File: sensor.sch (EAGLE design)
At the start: 16 parts

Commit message: sensor: pcb route completed
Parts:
- removed D1: (no value), SparkFun-DiscreteSemi:DIODESMA
- added SCHOTTKEY: 0, SparkFun-Resistors:10KOHM1/10W1%(0603)0603
- APDS1: device mylib:APDS-9008 -> librae:APDS-9008
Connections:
- net VCC: now also SCHOTTKEY.2; no longer D1.A
- net VDD: now also SCHOTTKEY.1; no longer D1.C
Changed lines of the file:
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@@
 </classes>
 <parts>
-<part name="APDS1" library="mylib" deviceset="APDS-9008" device=""/>
 <part name="MCP6001" library="SparkFun-AnalogIC" deviceset="OPA344" device=""/>
 <part name="C1" library="SparkFun-Capacitors" deviceset="1.0UF-16V-10%(0603)" device="" value="4.7uF"/>
@@
 <part name="R4" library="SparkFun-Resistors" deviceset="10KOHM1/10W1%(0603)" device="0603" value="100K"/>
 <part name="R5" library="SparkFun-Resistors" deviceset="10KOHM1/10W1%(0603)" device="0603" value="10K"/>
-<part name="D1" library="SparkFun-DiscreteSemi" deviceset="DIODE" device="SMA"/>
 <part name="R6" library="SparkFun-Resistors" deviceset="10KOHM1/10W1%(0603)" device="0603" value="3.3M">
 <attribute name="PROD_ID" value="RES-00824"/>
@@
 <part name="GND1" library="SparkFun-Aesthetics" deviceset="GND" device=""/>
 <part name="SUPPLY1" library="SparkFun-Aesthetics" deviceset="VCC" device=""/>
+<part name="SCHOTTKEY" library="SparkFun-Resistors" deviceset="10KOHM1/10W1%(0603)" device="0603" value="0">
+<attribute name="PROD_ID" value="RES-00824"/>
+<attribute name="VALUE" value="10K"/>
+</part>
+<part name="APDS1" library="librae" deviceset="APDS-9008" device=""/>
 </parts>
 <sheets>
@@
 </plain>
 <instances>
-<instance part="APDS1" gate="G$1" x="-38.1" y="17.78" rot="R90"/>
 <instance part="MCP6001" gate="G$1" x="45.72" y="10.16"/>
 <instance part="C1" gate="G$1" x="-7.62" y="-7.62"/>
@@
 <instance part="R4" gate="G$1" x="27.94" y="27.94" rot="R90"/>
 <instance part="R5" gate="G$1" x="10.16" y="27.94" rot="R270"/>
-<instance part="D1" gate="G$1" x="48.26" y="45.72" rot="R180"/>
 <instance part="R6" gate="G$1" x="43.18" y="38.1"/>
 <instance part="JP1" gate="G$1" x="81.28" y="48.26" rot="R180"/>
@@
 <instance part="GND1" gate="1" x="-7.62" y="-22.86"/>
 <instance part="SUPPLY1" gate="1" x="53.34" y="55.88"/>
+<instance part="SCHOTTKEY" gate="G$1" x="48.26" y="45.72"/>
+<instance part="APDS1" gate="G$1" x="-38.1" y="17.78" rot="R90"/>
 </instances>
 <busses>
@@
 <wire x1="-60.96" y1="50.8" x2="-78.74" y2="50.8" width="0.1524" layer="91"/>
 <wire x1="-78.74" y1="50.8" x2="-78.74" y2="20.32" width="0.1524" layer="91"/>
-<pinref part="D1" gate="G$1" pin="A"/>
 <wire x1="50.8" y1="45.72" x2="53.34" y2="45.72" width="0.1524" layer="91"/>
 <wire x1="53.34" y1="45.72" x2="53.34" y2="50.8" width="0.1524" layer="91"/>
@@
 <pinref part="SUPPLY1" gate="1" pin="VCC"/>
 <wire x1="53.34" y1="50.8" x2="53.34" y2="55.88" width="0.1524" layer="91"/>
+<pinref part="SCHOTTKEY" gate="G$1" pin="2"/>
 </segment>
 </net>
 <net name="VDD" class="0">
 <segment>
-<pinref part="APDS1" gate="G$1" pin="1"/>
 <wire x1="-43.18" y1="12.7" x2="-45.72" y2="12.7" width="0.1524" layer="91"/>
 <wire x1="-45.72" y1="12.7" x2="-45.72" y2="20.32" width="0.1524" layer="91"/>
-<pinref part="D1" gate="G$1" pin="C"/>
 <wire x1="-45.72" y1="20.32" x2="-45.72" y2="45.72" width="0.1524" layer="91"/>
-<wire x1="-45.72" y1="45.72" x2="45.72" y2="45.72" width="0.1524" layer="91"/>
+<wire x1="-45.72" y1="45.72" x2="43.18" y2="45.72" width="0.1524" layer="91"/>
 <pinref part="MCP6001" gate="G$1" pin="V+"/>
 <wire x1="45.72" y1="17.78" x2="45.72" y2="20.32" width="0.1524" layer="91"/>
 <wire x1="45.72" y1="20.32" x2="-45.72" y2="20.32" width="0.1524" layer="91"/>
 <junction x="-45.72" y="20.32"/>
+<pinref part="SCHOTTKEY" gate="G$1" pin="1"/>
+<pinref part="APDS1" gate="G$1" pin="1"/>
 </segment>
 </net>
@@
 <net name="N$7" class="0">
 <segment>
-<pinref part="APDS1" gate="G$1" pin="4"/>
 <wire x1="-30.48" y1="7.62" x2="-25.4" y2="7.62" width="0.1524" layer="91"/>
 <pinref part="C2" gate="G$1" pin="2"/>
@@
 <pinref part="R2" gate="G$1" pin="2"/>
 <wire x1="-25.4" y1="-2.54" x2="-25.4" y2="7.62" width="0.1524" layer="91"/>
+<pinref part="APDS1" gate="G$1" pin="4"/>
 </segment>
 </net>
@@
 <junction x="-45.72" y="-17.78"/>
 <wire x1="-45.72" y1="7.62" x2="-45.72" y2="-17.78" width="0.1524" layer="91"/>
-<pinref part="APDS1" gate="G$1" pin="3"/>
 <wire x1="-43.18" y1="7.62" x2="-45.72" y2="7.62" width="0.1524" layer="91"/>
 <wire x1="-25.4" y1="-17.78" x2="-7.62" y2="-17.78" width="0.1524" layer="91"/>
@@
 <junction x="-7.62" y="-17.78"/>
 <junction x="-25.4" y="-17.78"/>
-</segment>
-</net>
+<pinref part="APDS1" gate="G$1" pin="3"/>
+</segment>
+</net>

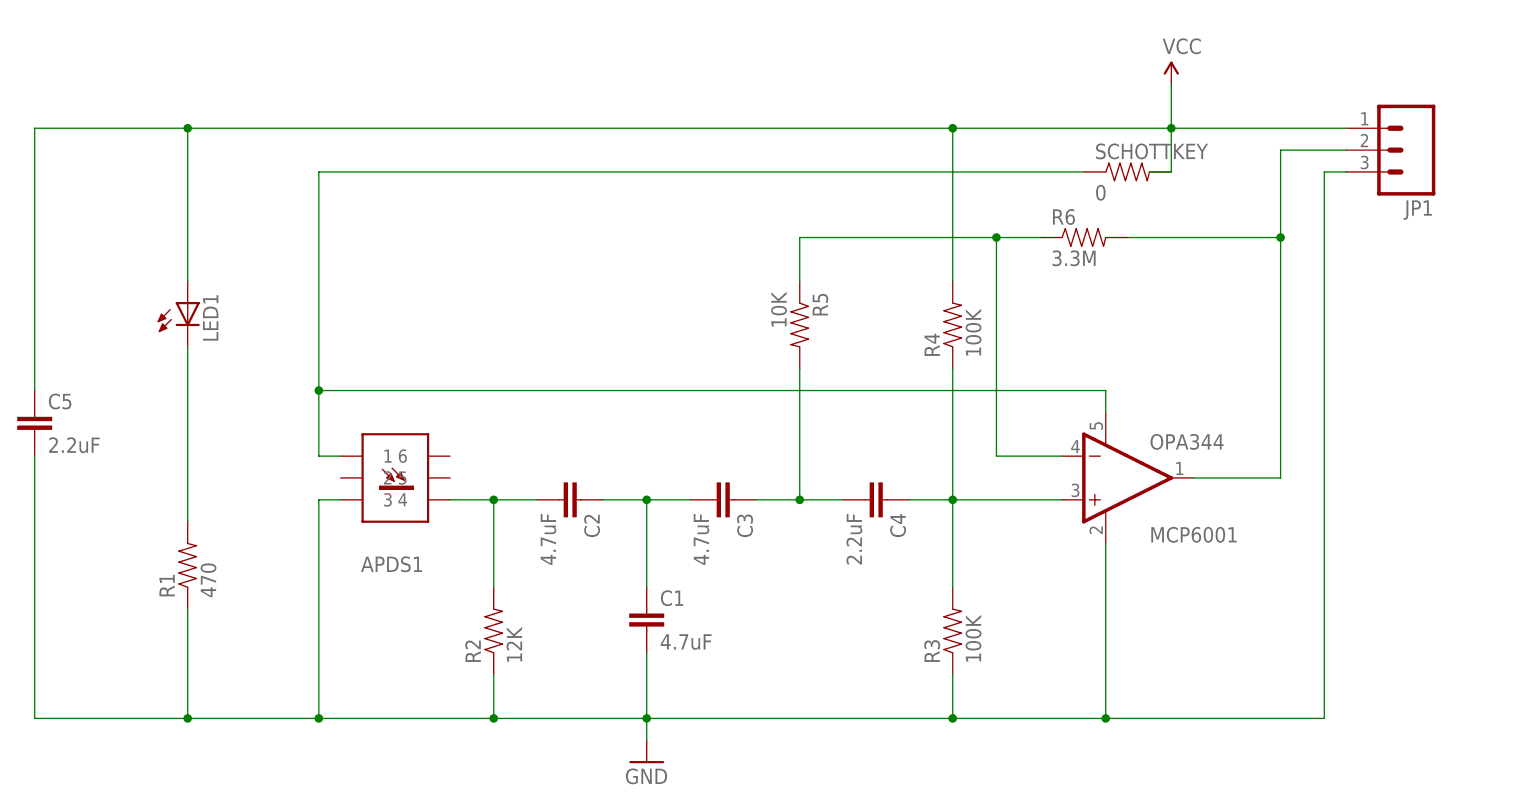
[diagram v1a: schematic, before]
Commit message: sensor: fix apds-9008 package error
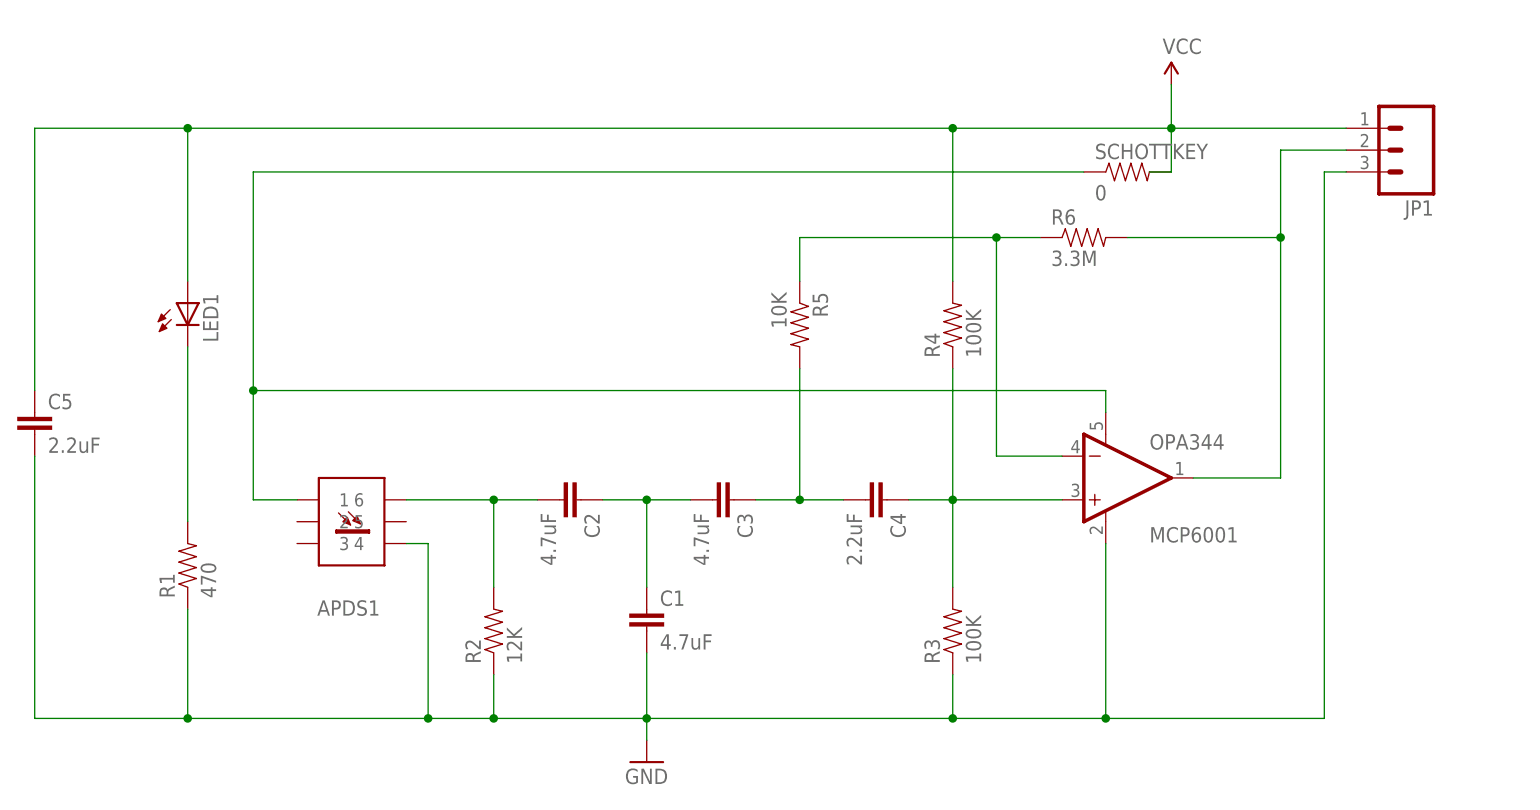
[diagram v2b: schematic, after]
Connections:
- net GND: now also APDS1.4; no longer APDS1.3
- net N$7: now also APDS1.6; no longer APDS1.4
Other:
- moved on the sheet: APDS1
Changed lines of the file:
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@@
 <instance part="SUPPLY1" gate="1" x="53.34" y="55.88"/>
 <instance part="SCHOTTKEY" gate="G$1" x="48.26" y="45.72"/>
-<instance part="APDS1" gate="G$1" x="-38.1" y="17.78" rot="R90"/>
+<instance part="APDS1" gate="G$1" x="-43.18" y="12.7" rot="R90"/>
 </instances>
 <busses>
@@
 <net name="VDD" class="0">
 <segment>
-<wire x1="-43.18" y1="12.7" x2="-45.72" y2="12.7" width="0.1524" layer="91"/>
-<wire x1="-45.72" y1="12.7" x2="-45.72" y2="20.32" width="0.1524" layer="91"/>
-<wire x1="-45.72" y1="20.32" x2="-45.72" y2="45.72" width="0.1524" layer="91"/>
-<wire x1="-45.72" y1="45.72" x2="43.18" y2="45.72" width="0.1524" layer="91"/>
+<wire x1="-48.26" y1="7.62" x2="-53.34" y2="7.62" width="0.1524" layer="91"/>
+<wire x1="-53.34" y1="7.62" x2="-53.34" y2="20.32" width="0.1524" layer="91"/>
+<wire x1="-53.34" y1="20.32" x2="-53.34" y2="45.72" width="0.1524" layer="91"/>
+<wire x1="-53.34" y1="45.72" x2="43.18" y2="45.72" width="0.1524" layer="91"/>
 <pinref part="MCP6001" gate="G$1" pin="V+"/>
 <wire x1="45.72" y1="17.78" x2="45.72" y2="20.32" width="0.1524" layer="91"/>
-<wire x1="45.72" y1="20.32" x2="-45.72" y2="20.32" width="0.1524" layer="91"/>
-<junction x="-45.72" y="20.32"/>
+<wire x1="45.72" y1="20.32" x2="-53.34" y2="20.32" width="0.1524" layer="91"/>
+<junction x="-53.34" y="20.32"/>
 <pinref part="SCHOTTKEY" gate="G$1" pin="1"/>
 <pinref part="APDS1" gate="G$1" pin="1"/>
@@
 <net name="N$7" class="0">
 <segment>
-<wire x1="-30.48" y1="7.62" x2="-25.4" y2="7.62" width="0.1524" layer="91"/>
 <pinref part="C2" gate="G$1" pin="2"/>
 <wire x1="-25.4" y1="7.62" x2="-20.32" y2="7.62" width="0.1524" layer="91"/>
-<junction x="-25.4" y="7.62"/>
 <pinref part="R2" gate="G$1" pin="2"/>
 <wire x1="-25.4" y1="-2.54" x2="-25.4" y2="7.62" width="0.1524" layer="91"/>
-<pinref part="APDS1" gate="G$1" pin="4"/>
+<pinref part="APDS1" gate="G$1" pin="6"/>
+<wire x1="-35.56" y1="7.62" x2="-25.4" y2="7.62" width="0.1524" layer="91"/>
+<junction x="-25.4" y="7.62"/>
 </segment>
 </net>
@@
 <pinref part="R2" gate="G$1" pin="1"/>
 <wire x1="-25.4" y1="-12.7" x2="-25.4" y2="-17.78" width="0.1524" layer="91"/>
-<wire x1="-25.4" y1="-17.78" x2="-45.72" y2="-17.78" width="0.1524" layer="91"/>
-<wire x1="-45.72" y1="-17.78" x2="-60.96" y2="-17.78" width="0.1524" layer="91"/>
-<junction x="-45.72" y="-17.78"/>
-<wire x1="-45.72" y1="7.62" x2="-45.72" y2="-17.78" width="0.1524" layer="91"/>
-<wire x1="-43.18" y1="7.62" x2="-45.72" y2="7.62" width="0.1524" layer="91"/>
+<wire x1="-25.4" y1="-17.78" x2="-33.02" y2="-17.78" width="0.1524" layer="91"/>
+<wire x1="-33.02" y1="-17.78" x2="-60.96" y2="-17.78" width="0.1524" layer="91"/>
 <wire x1="-25.4" y1="-17.78" x2="-7.62" y2="-17.78" width="0.1524" layer="91"/>
 <pinref part="C1" gate="G$1" pin="2"/>
@@
 <junction x="-7.62" y="-17.78"/>
 <junction x="-25.4" y="-17.78"/>
-<pinref part="APDS1" gate="G$1" pin="3"/>
+<pinref part="APDS1" gate="G$1" pin="4"/>
+<wire x1="-35.56" y1="2.54" x2="-33.02" y2="2.54" width="0.1524" layer="91"/>
+<wire x1="-33.02" y1="2.54" x2="-33.02" y2="-17.78" width="0.1524" layer="91"/>
+<junction x="-33.02" y="-17.78"/>
 </segment>
 </net>

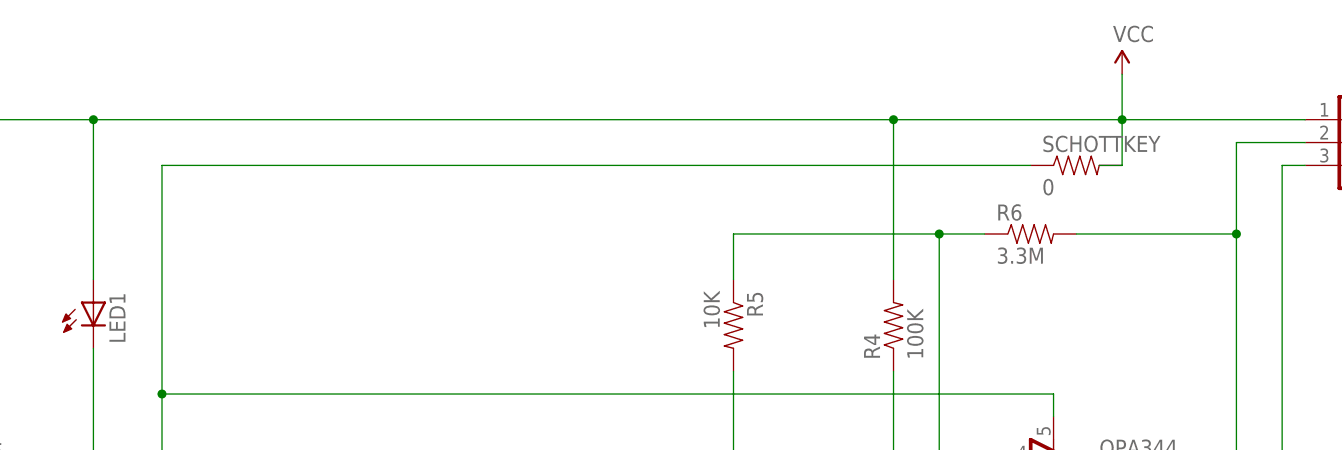
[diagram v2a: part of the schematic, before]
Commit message: sensor: correct schematic and refine layout
1. Replace fake schottkey with a *real* one.
2. Refine polygon.
3. Refine dimension.
4. Refine panel.
5. Add more blowholes (vias).
6. Slightly refine some wires.
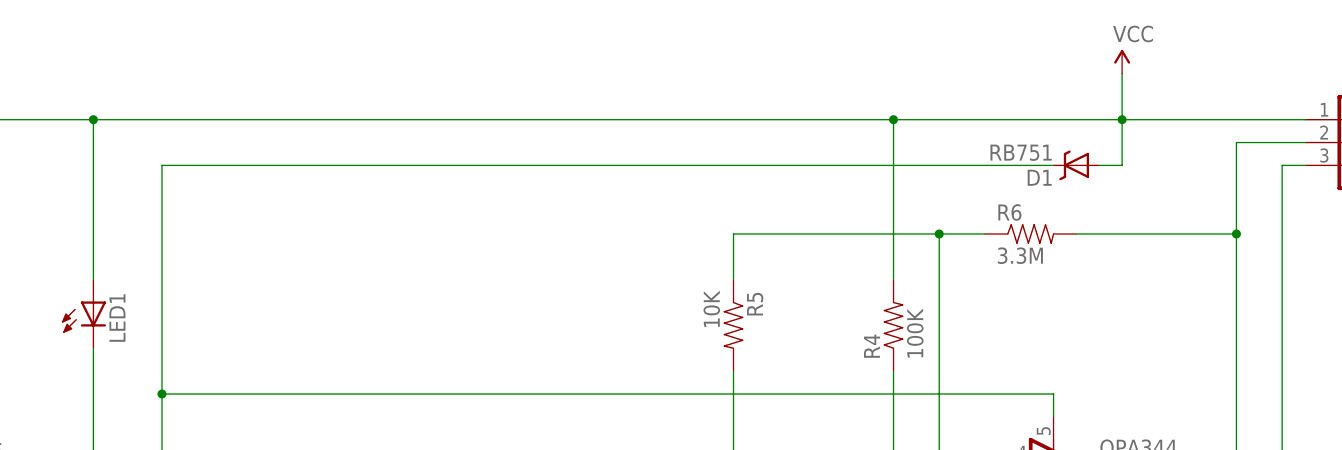
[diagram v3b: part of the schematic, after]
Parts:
- removed SCHOTTKEY: 0, SparkFun-Resistors:10KOHM1/10W1%(0603)0603
- added D1: RB751, SparkFun-DiscreteSemi:RB751
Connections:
- net VCC: now also D1.A; no longer SCHOTTKEY.2
- net VDD: now also D1.C; no longer SCHOTTKEY.1
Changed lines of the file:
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@@
 <setting verticaltext="up"/>
 </settings>
-<grid distance="0.1" unitdist="inch" unit="inch" style="lines" multiple="1" display="yes" altdistance="0.01" altunitdist="inch" altunit="inch"/>
+<grid distance="0.1" unitdist="inch" unit="inch" style="lines" multiple="1" display="no" altdistance="0.01" altunitdist="inch" altunit="inch"/>
 <layers>
 <layer number="1" name="Top" color="4" fill="1" visible="no" active="no"/>
@@
 <part name="GND1" library="SparkFun-Aesthetics" deviceset="GND" device=""/>
 <part name="SUPPLY1" library="SparkFun-Aesthetics" deviceset="VCC" device=""/>
-<part name="SCHOTTKEY" library="SparkFun-Resistors" deviceset="10KOHM1/10W1%(0603)" device="0603" value="0">
-<attribute name="PROD_ID" value="RES-00824"/>
-<attribute name="VALUE" value="10K"/>
-</part>
 <part name="APDS1" library="librae" deviceset="APDS-9008" device=""/>
+<part name="D1" library="SparkFun-DiscreteSemi" deviceset="RB751" device="" value="RB751"/>
 </parts>
 <sheets>
@@
 <instance part="GND1" gate="1" x="-7.62" y="-22.86"/>
 <instance part="SUPPLY1" gate="1" x="53.34" y="55.88"/>
-<instance part="SCHOTTKEY" gate="G$1" x="48.26" y="45.72"/>
 <instance part="APDS1" gate="G$1" x="-43.18" y="12.7" rot="R90"/>
+<instance part="D1" gate="G$1" x="48.26" y="45.72" rot="R180"/>
 </instances>
 <busses>
@@
 <pinref part="SUPPLY1" gate="1" pin="VCC"/>
 <wire x1="53.34" y1="50.8" x2="53.34" y2="55.88" width="0.1524" layer="91"/>
-<pinref part="SCHOTTKEY" gate="G$1" pin="2"/>
+<pinref part="D1" gate="G$1" pin="A"/>
 </segment>
 </net>
@@
 <wire x1="-53.34" y1="7.62" x2="-53.34" y2="20.32" width="0.1524" layer="91"/>
 <wire x1="-53.34" y1="20.32" x2="-53.34" y2="45.72" width="0.1524" layer="91"/>
-<wire x1="-53.34" y1="45.72" x2="43.18" y2="45.72" width="0.1524" layer="91"/>
+<wire x1="-53.34" y1="45.72" x2="45.72" y2="45.72" width="0.1524" layer="91"/>
 <pinref part="MCP6001" gate="G$1" pin="V+"/>
 <wire x1="45.72" y1="17.78" x2="45.72" y2="20.32" width="0.1524" layer="91"/>
 <wire x1="45.72" y1="20.32" x2="-53.34" y2="20.32" width="0.1524" layer="91"/>
 <junction x="-53.34" y="20.32"/>
-<pinref part="SCHOTTKEY" gate="G$1" pin="1"/>
 <pinref part="APDS1" gate="G$1" pin="1"/>
+<pinref part="D1" gate="G$1" pin="C"/>
 </segment>
 </net>
